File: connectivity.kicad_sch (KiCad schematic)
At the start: 56 parts, among them CN1 GPS_Port, CN2 SM06B-GHS-TB(LF)(SN), Con2 DS1023-1X2SF11, Con3 DS1023-1X10SF11, Con4 DS1023-1X6SF11, J1 USB_C_Receptacle, J10 DS1023-1X5SF11, J11 DS1023-1X5SF11, J12 DS1023-1X5SF11, J13 DS1023-1X5SF11, J14 DS1023-1X5SF11, J2 DS1023-1X9S21, J3 DS1023-1X7SF11, J4 DS1023-1X8SF11, J5 DS1023-1X6SF11, J6 DS1023-1X6SF11, J7 DS1023-1X8SF11, J8 DS1023-1X8SF11, J9 DS1023-1X5SF11, U3 FT232RL, con1 DS1023-1X3SF11

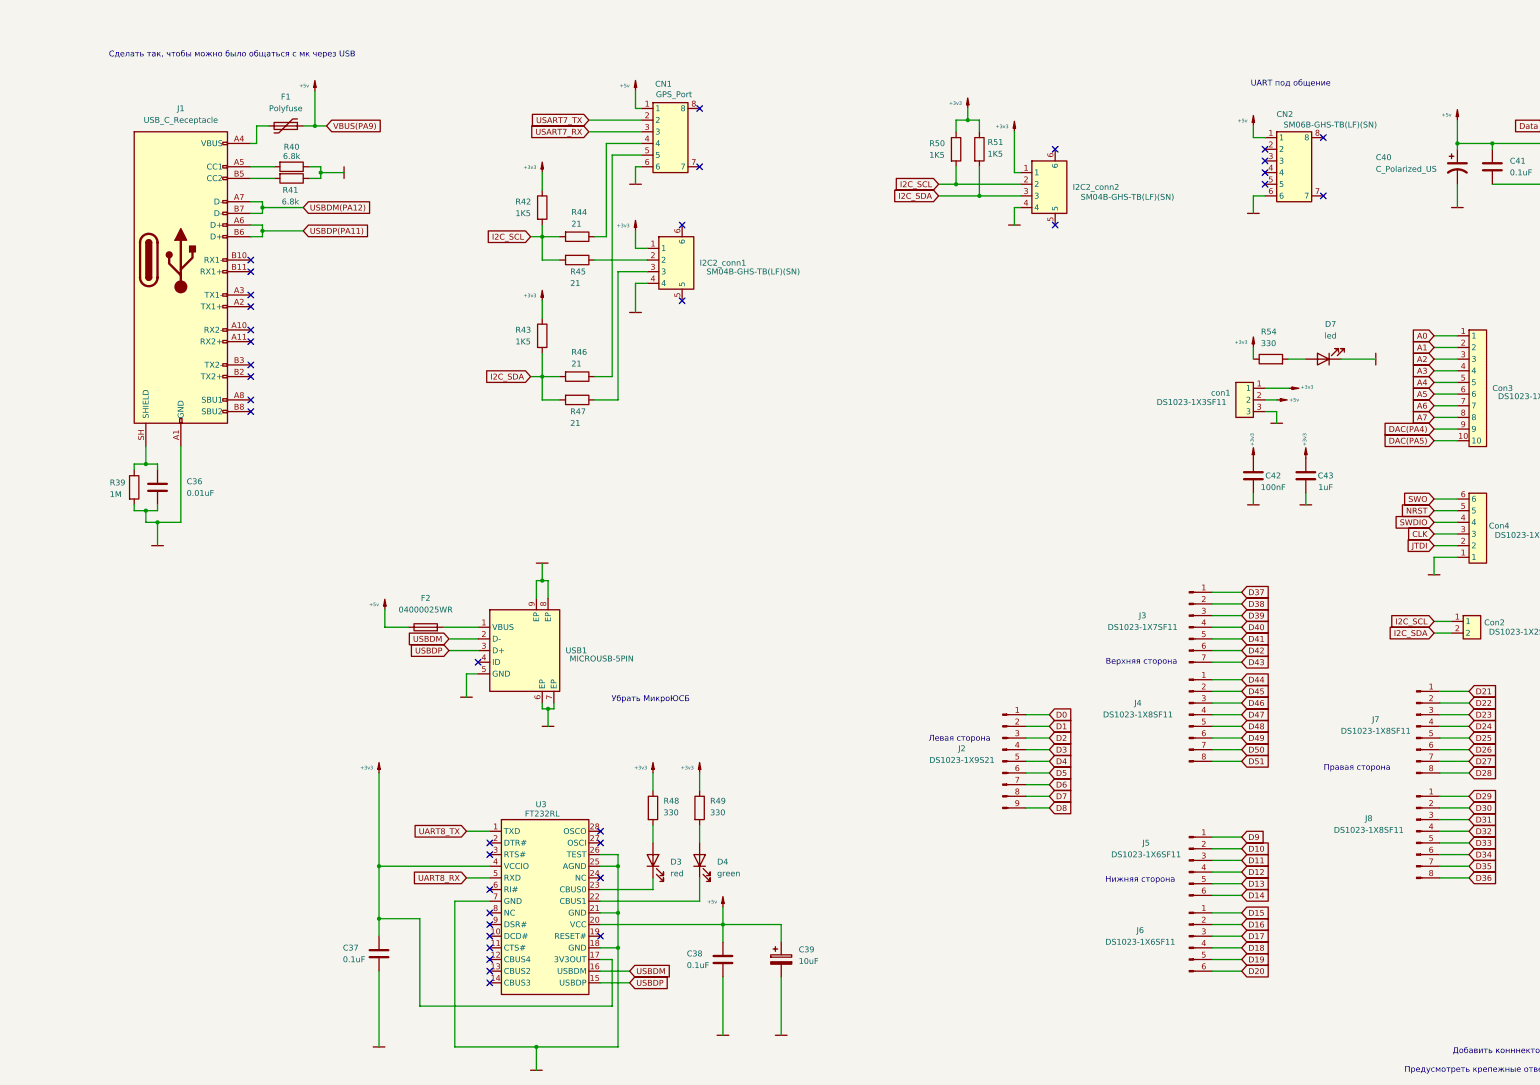
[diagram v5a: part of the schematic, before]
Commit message: edit pins shem plat_logic
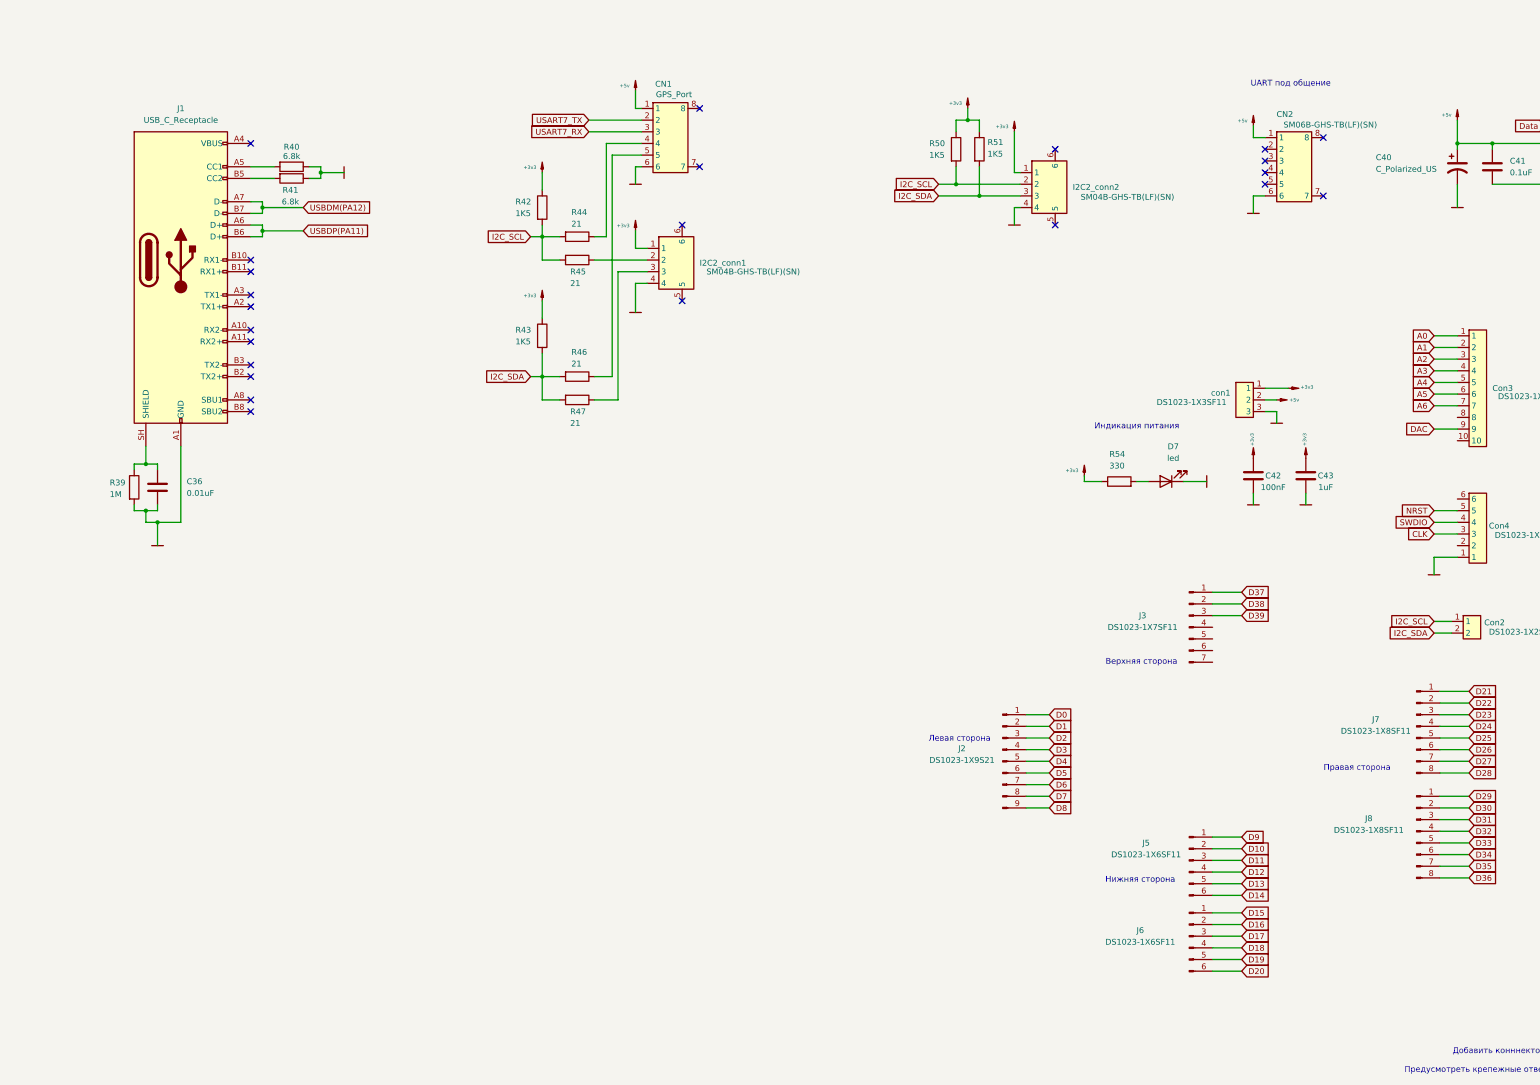
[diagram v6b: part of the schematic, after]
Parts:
- removed C37, C38: 0.1uF, Capacitor_SMD:C_0603_1608Metric, symbol Device:C
- removed C39: 10uF, Capacitor_SMD:C_0603_1608Metric, symbol Device:C_Polarized
- removed D3: red, LED_SMD:LED_0603_1608Metric, symbol Device:LED
- removed D4: green, LED_SMD:LED_0603_1608Metric, symbol Device:LED
- removed F1: Polyfuse, Fuse:Fuse_0603_1608Metric, symbol Device:Polyfuse
- removed F2: 04000025WR, Fuse:Fuse_0603_1608Metric, symbol Device:Fuse
- removed J4: DS1023-1X8SF11, Connector_PinHeader_2.54mm:PinHeader_1x08_P2.54mm_Vertical, symbol Connector:Conn_01x08_Pin
- removed R48, R49: 330, Resistor_SMD:R_0805_2012Metric, symbol Device:R
- removed U3: FT232RL, Package_SO:SSOP-28_5.3x10.2mm_P0.65mm, symbol MyLIB:FT232RL
- removed USB1: MICROUSB-5PIN, Connector_USB:USB_Micro-B_GCT_USB3076-30-A, symbol MyLIB:microUSB
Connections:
- net A7: no longer names the net of Con3.8
- net D40: no longer names the net of J3.4 (Pin_4)
- net D41: no longer names the net of J3.5 (Pin_5)
- net D42: no longer names the net of J3.6 (Pin_6)
- net D43: no longer names the net of J3.7 (Pin_7)
- net DAC(PA4) renamed DAC
- net DAC(PA5): no longer names the net of Con3.10
- net JTDI: no longer names the net of Con4.2
- net SWO: no longer names the net of Con4.6
- no-connect marks 37 -> 23
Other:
- note added: "Индикация питания"
- note removed: "Сделать так, чтобы можно было общаться с мк через USB"
- note removed: "Убрать МикроЮСБ"
- moved on the sheet: D7, R54

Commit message: edit princip shem
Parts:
- removed CN2: SM06B-GHS-TB(LF)(SN), Connector_JST:JST_GH_SM06B-GHS-TB_1x06-1MP_P1.25mm_Horizontal, symbol MyLIB:SM_06B_GHS_TB
- removed Con3: DS1023-1X10SF11, Connector_PinHeader_2.54mm:PinHeader_1x10_P2.54mm_Vertical, symbol MyLIB:DS1023-1X10SF11
- removed Con4: DS1023-1X6SF11, Connector_PinHeader_2.54mm:PinHeader_1x06_P2.54mm_Vertical, symbol MyLIB:Con
- removed J2: DS1023-1X9S21, Connector_PinHeader_2.54mm:PinHeader_1x09_P2.54mm_Vertical, symbol Connector:Conn_01x09_Pin
- removed J3: DS1023-1X7SF11, Connector_PinHeader_2.54mm:PinHeader_1x07_P2.54mm_Vertical, symbol Connector:Conn_01x07_Pin
- removed J5, J6: DS1023-1X6SF11, Connector_PinHeader_2.54mm:PinHeader_1x06_P2.54mm_Vertical, symbol Connector:Conn_01x06_Pin
- removed J7, J8: DS1023-1X8SF11, Connector_PinHeader_2.54mm:PinHeader_1x08_P2.54mm_Vertical, symbol Connector:Conn_01x08_Pin
- removed con1: DS1023-1X3SF11, Connector_PinHeader_2.54mm:PinHeader_1x03_P2.54mm_Vertical, symbol MyLIB:con_3
- added C44: 100nF, Capacitor_SMD:C_0603_1608Metric, symbol Device:C
- added Con4: DS1023-1X5SF11, Connector_PinHeader_2.54mm:PinHeader_1x05_P2.54mm_Vertical, symbol Connectors_kl:CONN_5
- added I2C2_conn3, I2C2_conn4: SM04B-GHS-TB(LF)(SN), Connector_JST:JST_GH_SM04B-GHS-TB_1x04-1MP_P1.25mm_Horizontal, symbol MyLIB:I2C_connector
- added J2: DS1023-1X6SF11, Connector_PinHeader_2.54mm:PinHeader_1x06_P2.54mm_Vertical, symbol Connector:Conn_01x06_Pin
- added J3: DS1023-1X8SF11, Connector_PinHeader_2.54mm:PinHeader_1x08_P2.54mm_Vertical, symbol Connector:Conn_01x08_Pin
- added J4, J5, J6: DS1023-1X11S21, Connector_PinHeader_2.54mm:PinHeader_1x11_P2.54mm_Vertical, symbol Connector:Conn_01x11_Pin
- added JP3: Jumper_2_Open, Jumper:SolderJumper-2_P1.3mm_Open_Pad1.0x1.5mm, symbol Jumper:Jumper_2_Open
- added R20, R34: 10k, Resistor_SMD:R_0603_1608Metric, symbol Device:R
- added R38: 120, Resistor_SMD:R_0603_1608Metric, symbol Device:R
- added R55, R56: 1K5, Resistor_SMD:R_0805_2012Metric, symbol Device:R
- added U3: SN65HVD232, Package_SO:SOIC-8_3.9x4.9mm_P1.27mm, symbol Interface_CAN_LIN:SN65HVD232
- added XL1, XL2, XL3, XL4: JST_GH_SM06B-GHS-TB, Connector_JST:JST_GH_SM05B-GHS-TB_1x05-1MP_P1.25mm_Horizontal, symbol Connectors_kl:CONN_5
- added con1: DS1023-1X3SF11, Connector_PinHeader_2.54mm:PinHeader_1x03_P2.54mm_Vertical, symbol Connector:Conn_01x03_Pin
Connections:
- net D48 is gone; now on net D38: R53.1
- net D49 is gone; now on net D37: R52.1
- net +3v3: now also C44.1, Con4.1, I2C2_conn4.1, R20.1, R34.1, R55.1, R56.1, U3.3 (VCC), XL1.1, XL2.1, XL3.1, XL4.1, con1.1 (Pin_1)
- net +5v: now also I2C2_conn3.1, con1.2 (Pin_2)
- net A0: now also J3.1 (Pin_1)
- net A1: now also J3.2 (Pin_2)
- net A2: now also J3.3 (Pin_3)
- net A3: now also J3.4 (Pin_4)
- net A4: now also J3.5 (Pin_5)
- net A5: now also J3.6 (Pin_6)
- net A6: now also J3.7 (Pin_7)
- net CLK: now also Con4.4
- net D0: now also J4.1 (Pin_1)
- net D1: now also J4.2 (Pin_2)
- net D10: now also J4.11 (Pin_11)
- net D11: now also J5.1 (Pin_1)
- net D12: now also J5.2 (Pin_2)
- net D13: now also J5.3 (Pin_3)
- net D14: now also J5.4 (Pin_4)
- net D15: now also J5.5 (Pin_5)
- net D16: now also J5.6 (Pin_6)
- net D17: now also J5.7 (Pin_7)
- net D18: now also J5.8 (Pin_8)
- net D19: now also J5.9 (Pin_9)
- net D2: now also J4.3 (Pin_3)
- net D20: now also J5.10 (Pin_10)
- net D21: now also J5.11 (Pin_11)
- net D22: now also J6.1 (Pin_1)
- net D23: now also J6.2 (Pin_2)
- net D24: now also J6.3 (Pin_3)
- net D25: now also J6.4 (Pin_4)
- net D26: now also J6.5 (Pin_5)
- net D27: now also J6.6 (Pin_6)
- net D28: now also J6.7 (Pin_7)
- net D29: now also J6.8 (Pin_8)
- net D3: now also J4.4 (Pin_4)
- net D30: now also J6.9 (Pin_9)
- net D31: now also J6.10 (Pin_10)
- net D32: now also J6.11 (Pin_11)
- net D33: now also J2.1 (Pin_1)
- net D34: now also J2.2 (Pin_2)
- net D35: now also J2.3 (Pin_3)
- net D36: now also J2.4 (Pin_4)
- net D37: now also J2.5 (Pin_5)
- net D38: now also J2.6 (Pin_6)
- net D4: now also J4.5 (Pin_5)
- net D5: now also J4.6 (Pin_6)
- net D6: now also J4.7 (Pin_7)
- net D7: now also J4.8 (Pin_8)
- net D8: now also J4.9 (Pin_9)
- net D9: now also J4.10 (Pin_10)
- net DAC: now also J3.8 (Pin_8)
- net GND: now also C44.2, Con4.5, I2C2_conn3.4, I2C2_conn4.4, U3.2 (GND), XL1.5, XL2.5, XL3.5, XL4.5, con1.3 (Pin_3)
- net NRST: now also Con4.2
- net SWDIO: now also Con4.3
- net I2C_SCL renamed I2C1_SCL
- net I2C1_SCL: no longer Con2.1, I2C2_conn2.2, R50.2
- net I2C_SDA renamed I2C1_SDA
- net I2C1_SDA: no longer Con2.2, I2C2_conn2.3, R51.2
- net USART7_RX renamed USART1_RX
- net USART7_TX renamed USART1_TX
- net USBDM(PA12) renamed USB_DM
- net USBDP(PA11) renamed USB_DP
- new net: I2C2_conn4.3, JP3.2 (B), U3.6 (CANL)
- new net: I2C2_conn4.2, R38.1, U3.7 (CANH)
- new net: JP3.1 (A), R38.2
- new net CAN1_RX: U3.4 (R)
- new net CAN1_TX: U3.1 (D)
- new net I2C2_SDA: I2C2_conn2.3, R51.2
- new net I2C2_SLC: I2C2_conn2.2, R50.2
- new net I2C3_SCL: Con2.1, R55.2
- new net I2C3_SDA: Con2.2, R56.2
- new net SDIO_CK: XL4.3
- new net SDIO_CMD: R20.2, XL4.4
- new net SDIO_D0: R34.2, XL4.2
- new net SPI1_MISO: XL3.3
- new net SPI1_MOSI: XL3.4
- new net SPI1_SCK: XL3.2
- new net SPI3_MISO: XL1.3
- new net SPI3_MOSI: XL1.4
- new net SPI3_SCK: XL1.2
- new net SPI4_MISO: XL2.3
- new net SPI4_MOSI: XL2.4
- new net SPI4_SCK: XL2.2
- new net UART8_RX: I2C2_conn3.3
- new net UART8_TX: I2C2_conn3.2
- no-connect marks 23 -> 21
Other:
- note added: "Верхняя сторона D33 - D38"
- note added: "Левая сторона D0 - D10"
- note added: "Нижняя сторона D11 - D21"
- note added: "Правая сторона D22 - D32"
- note added: "С силовой платы"
- note removed: "UART под общение"
- note removed: "Верхняя сторона"
- note removed: "Левая сторона"
- note removed: "Нижняя сторона"
- note removed: "Правая сторона"
- moved on the sheet: C40, C41, C42, C43, Con2, D5, D6, D7, DynamixelCon1, I2C2_conn2, J10, J11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

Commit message: Very sad. Need new place
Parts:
- removed Con4: DS1023-1X5SF11, Connector_PinHeader_2.54mm:PinHeader_1x05_P2.54mm_Vertical, symbol Connectors_kl:CONN_5
- removed XL1, XL2, XL3, XL4: JST_GH_SM06B-GHS-TB, Connector_JST:JST_GH_SM05B-GHS-TB_1x05-1MP_P1.25mm_Horizontal, symbol Connectors_kl:CONN_5
- added J11: DS1023-1X5SF11, Connector_PinHeader_2.54mm:PinHeader_1x05_P2.54mm_Vertical, symbol Connector:Conn_01x05_Pin
- added J2, J3, J4, J5: JST_GH_SM06B-GHS-TB, Connector_JST:JST_GH_SM05B-GHS-TB_1x05-1MP_P1.25mm_Horizontal, symbol Connector:Conn_01x05_Pin
- renumbered C36 to C34, C44 to C35, C40 to C36, C41 to C37, C42 to C38, C43 to C39, D7 to D3, D5 to D4, D6 to D5, I2C2_conn3 to I2C2_conn1, I2C2_conn4 to I2C2_conn2, I2C2_conn1 to I2C2_conn3, I2C2_conn2 to I2C2_conn4, J3 to J10, J9 to J12, J10 to J13, J11 to J14, J12 to J15, J13 to J16, J14 to J17, J4 to J6, J5 to J7, J2 to J8, J6 to J9, R39 to R36, R40 to R37, R41 to R38, R34 to R39, R20 to R40, R42 to R41, R43 to R42, R38 to R43, R50 to R48, R51 to R49, R52 to R50, R53 to R51, R54 to R52, R55 to R53, R56 to R54
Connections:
- net +3v3: now also J11.1 (Pin_1), J2.1 (Pin_1), J3.1 (Pin_1), J4.1 (Pin_1), J5.1 (Pin_1)
- net CLK: now also J11.2 (Pin_2)
- net GND: now also J11.5 (Pin_5), J2.5 (Pin_5), J3.5 (Pin_5), J4.5 (Pin_5), J5.5 (Pin_5)
- net NRST: now also J11.4 (Pin_4)
- net SDIO_CK: now also J2.3 (Pin_3)
- net SDIO_CMD: now also R39.2, J2.4 (Pin_4); no longer R40.2
- net SDIO_D0: now also R40.2, J2.2 (Pin_2); no longer R39.2
- net SPI1_MISO: now also J3.3 (Pin_3)
- net SPI1_MOSI: now also J3.4 (Pin_4)
- net SPI1_SCK: now also J3.2 (Pin_2)
- net SPI3_MISO: now also J4.3 (Pin_3)
- net SPI3_MOSI: now also J4.4 (Pin_4)
- net SPI3_SCK: now also J4.2 (Pin_2)
- net SPI4_MISO: now also J5.3 (Pin_3)
- net SPI4_MOSI: now also J5.4 (Pin_4)
- net SPI4_SCK: now also J5.2 (Pin_2)
- net SWDIO: now also J11.3 (Pin_3)
- net at JP3.2 (B), U3.6 (CANL): now also I2C2_conn2.2; no longer I2C2_conn2.3
- net at R43.1, U3.7 (CANH): now also I2C2_conn2.3; no longer I2C2_conn2.2
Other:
- moved on the sheet: R39, R40
